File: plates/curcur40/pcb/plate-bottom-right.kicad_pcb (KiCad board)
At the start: 2 copper layers, 125.1 x 92.6 mm, 0 parts

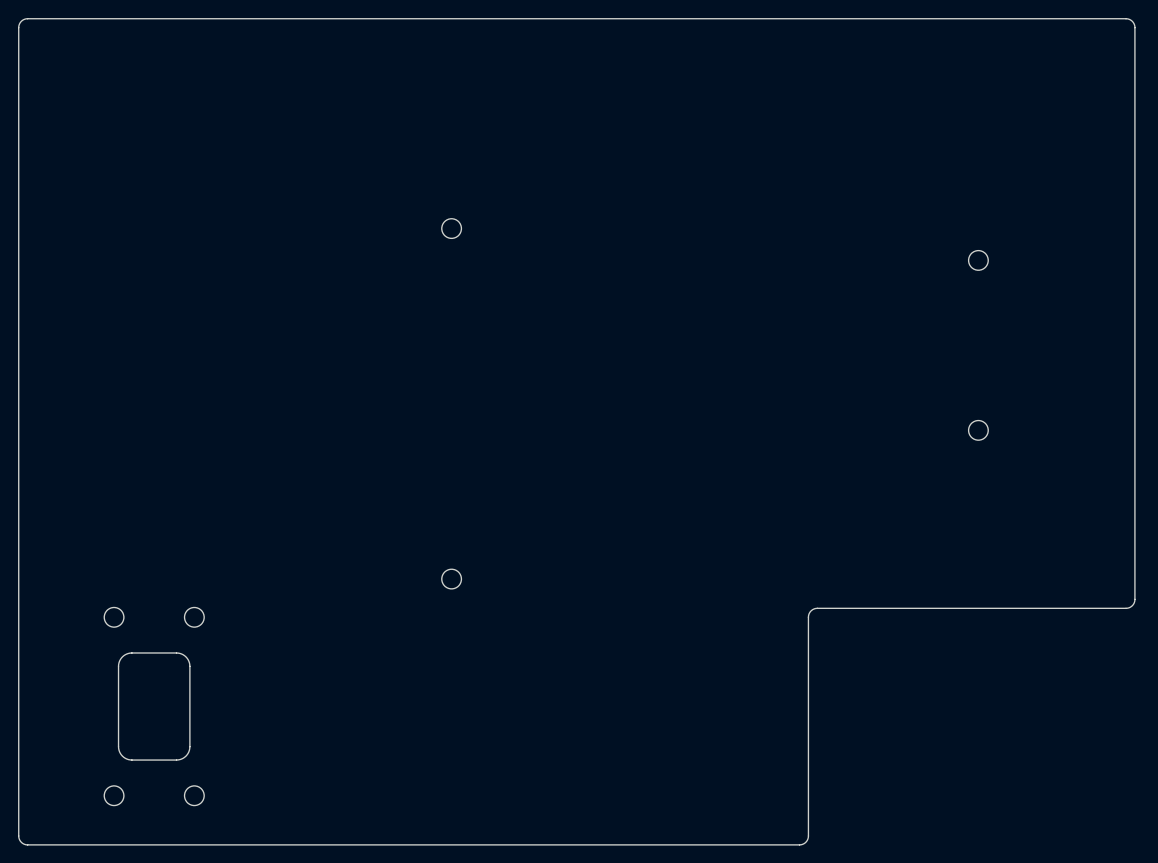
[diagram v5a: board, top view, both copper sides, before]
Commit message: Restore TRRS cutouts and relocate mounting holes to perimeter
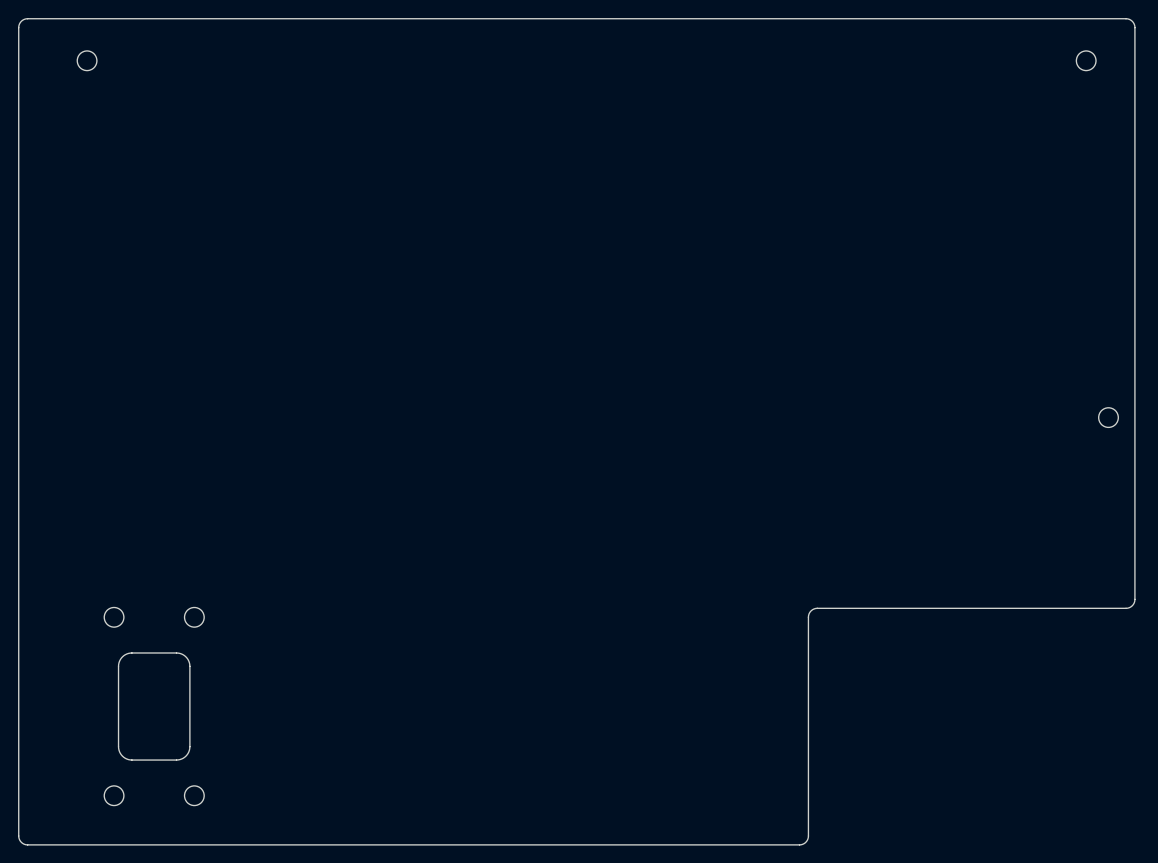
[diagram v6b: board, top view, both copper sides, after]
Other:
- outline, holes or cut-outs redrawn
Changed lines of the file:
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@@
+	)
+	(gr_circle
+		(center 2 -20)
+		(end 3.1 -20)
+		(stroke
+			(width 0.15)
+			(type default)
+		)
+		(fill no)
+		(layer "Edge.Cuts")
 	)
 	(gr_circle
@@
 		(layer "Edge.Cuts")
 	)
-	(gr_circle
-		(center 42.8625 -1.190625)
-		(end 43.9625 -1.190625)
-		(stroke
-			(width 0.15)
-			(type default)
-		)
-		(fill no)
-		(layer "Edge.Cuts")
-	)
-	(gr_circle
-		(center 42.8625 38.1)
-		(end 43.9625 38.1)
-		(stroke
-			(width 0.15)
-			(type default)
-		)
-		(fill no)
-		(layer "Edge.Cuts")
-	)
 	(gr_line
 		(start 81.8625 67.9)
@@
 	)
 	(gr_circle
-		(center 101.9175 2.38125)
-		(end 103.0175 2.38125)
+		(center 114 -20)
+		(end 115.1 -20)
 		(stroke
 			(width 0.15)
@@
 	)
 	(gr_circle
-		(center 101.9175 21.43125)
-		(end 103.0175 21.43125)
+		(center 116.5 20)
+		(end 117.6 20)
 		(stroke
 			(width 0.15)

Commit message: fix trrs top plate
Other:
- outline, holes or cut-outs redrawn
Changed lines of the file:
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@@
-	)
-	(gr_circle
-		(center 2 -20)
-		(end 3.1 -20)
-		(stroke
-			(width 0.15)
-			(type default)
-		)
-		(fill no)
-		(layer "Edge.Cuts")
 	)
 	(gr_circle
@@
 		(layer "Edge.Cuts")
 	)
+	(gr_circle
+		(center 23.8125 -22.5)
+		(end 24.9125 -22.5)
+		(stroke
+			(width 0.15)
+			(type default)
+		)
+		(fill no)
+		(layer "Edge.Cuts")
+	)
 	(gr_line
 		(start 81.8625 67.9)
@@
 	)
 	(gr_circle
-		(center 114 -20)
-		(end 115.1 -20)
+		(center 98 38)
+		(end 99.1 38)
 		(stroke
 			(width 0.15)
@@
 	)
 	(gr_circle
-		(center 116.5 20)
-		(end 117.6 20)
+		(center 100 -22.5)
+		(end 101.1 -22.5)
 		(stroke
 			(width 0.15)

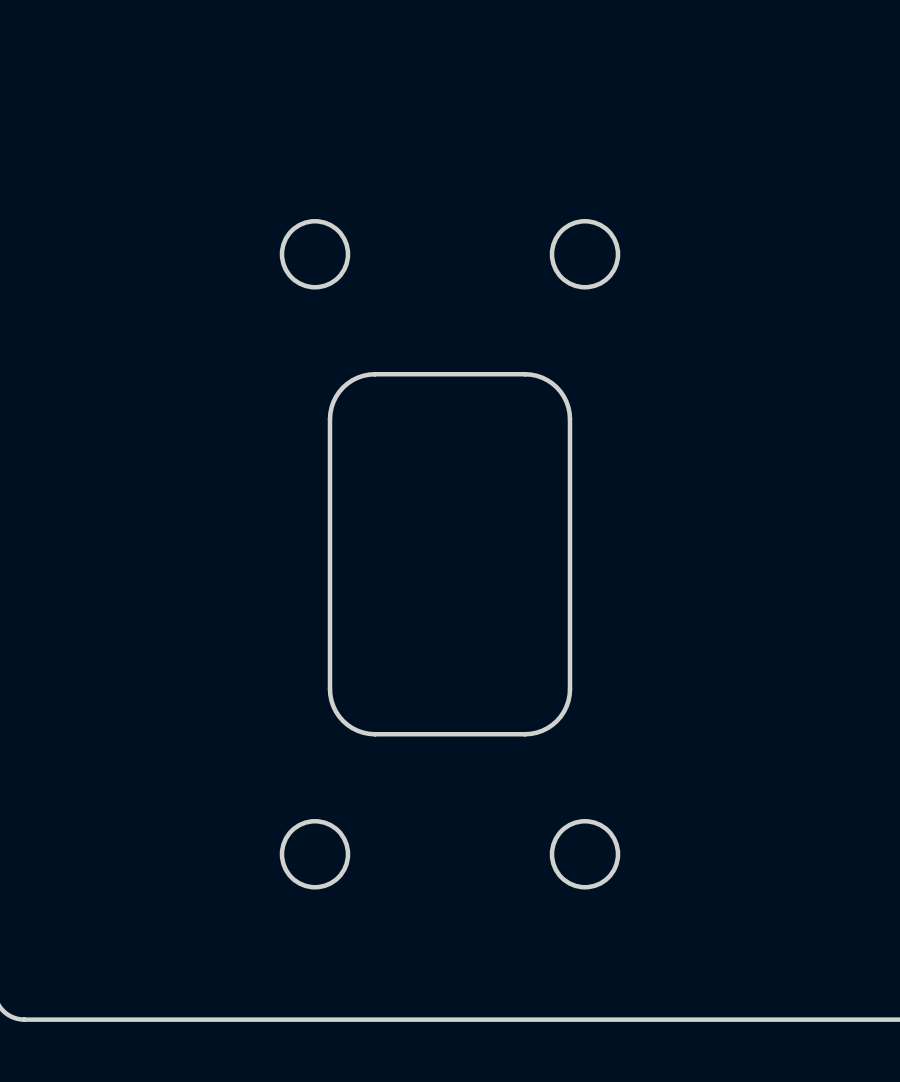
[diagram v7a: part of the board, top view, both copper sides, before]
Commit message: 🔴 1. 致命的な不具合（Critical：物理的に組立不可、または動作不可）
[Critical-1] トラックボール部の3D機構・光学設計の破綻（4重の物理的干渉・焦点外れ）
[Critical-2] 左右メイン基板の取付穴径が ∅2.20 mm になっており、M2スペーサーが貫通できない
[Critical-3] 3Dプリントケース内部の 2.0mm スペーサー受けボスが消失しており、高さが 2.0 mm 合わない
[Critical-4] PMW3360 センサー基板のプルアップ抵抗 R1（10kΩ）が PCBA の BOM/CPL から除外されており、リセット端子（NRESET）がフローティング（不定）になる
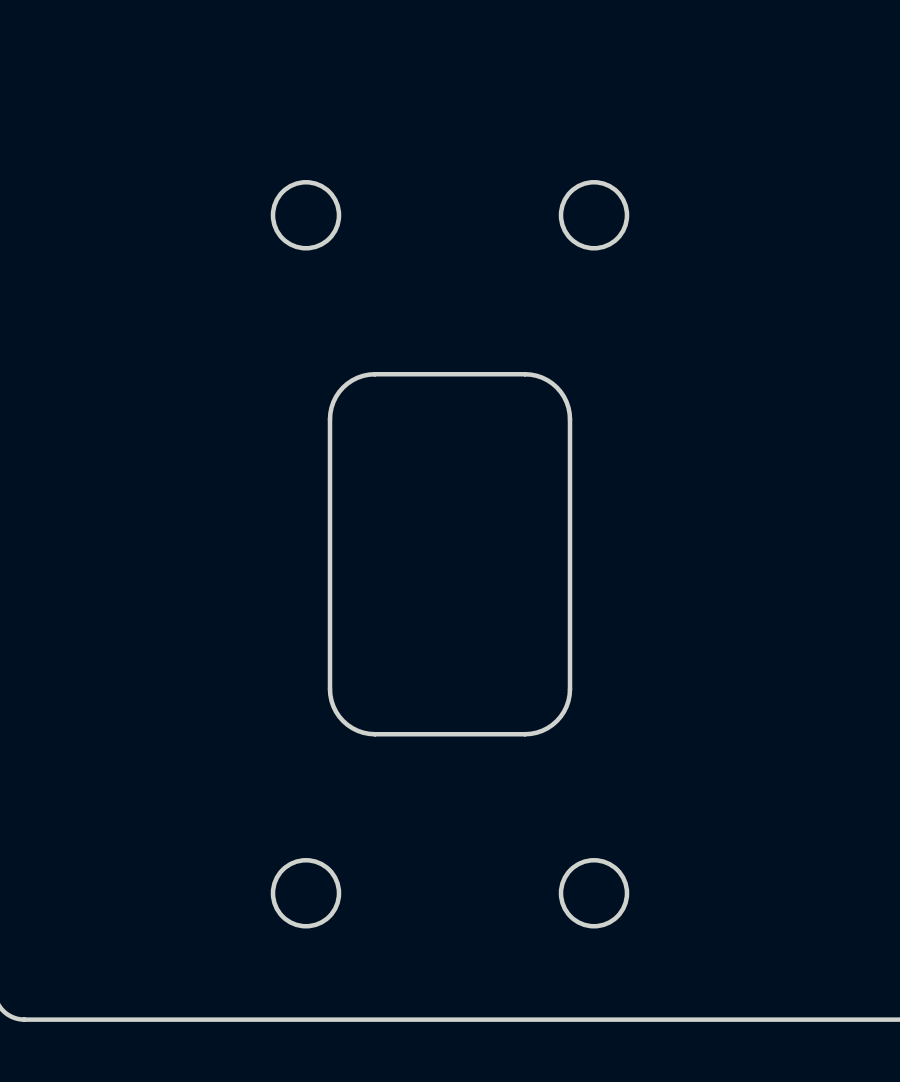
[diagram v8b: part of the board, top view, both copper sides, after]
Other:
- outline, holes or cut-outs redrawn
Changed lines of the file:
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@@
 	)
 	(gr_circle
-		(center 5.025 42.3875)
-		(end 6.125 42.3875)
+		(center 4.725 41.0875)
+		(end 5.825 41.0875)
 		(stroke
 			(width 0.15)
@@
 	)
 	(gr_circle
-		(center 5.025 62.3875)
-		(end 6.125 62.3875)
+		(center 4.725 63.6875)
+		(end 5.825 63.6875)
 		(stroke
 			(width 0.15)
@@
 	)
 	(gr_circle
-		(center 14.025 42.3875)
-		(end 15.125 42.3875)
+		(center 14.325 41.0875)
+		(end 15.424999 41.0875)
 		(stroke
 			(width 0.15)
@@
 	)
 	(gr_circle
-		(center 14.025 62.3875)
-		(end 15.125 62.3875)
+		(center 14.325 63.6875)
+		(end 15.424999 63.6875)
 		(stroke
 			(width 0.15)
